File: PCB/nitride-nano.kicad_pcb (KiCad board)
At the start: 6 copper layers, 120 x 57 mm, 323 parts, among them J3 XT-90-M, J4 SWD, J5 SSD1306, J6 XT90-F, P1 USB_C_Plug_USB2.0, Q1 EPC2367, Q10 SQJB90EP-T1_GE3, Q11 AO3404A, Q12 HUASHUO HSBB0115, Q13 AO3404A, Q2 EPC2367, Q3 EPC2367, Q4 EPC2367, Q5 HUASHUO HSBB0115, Q6 AGM612AP, Q8 AO3404A, Q9 AO3404A, SW1 EC11E15244G1, U1 LT8390AIUFD-PBF, U10 SN74LVC1G17DBVR, U11 LMR16006XDDCR, U12 FT234XD, U13 LMR16006XDDCR, U2 STM32G474CEUx, U3 TPD4S480RUKR, U4 TPS26750SRSMR, U5 LM2765, U6 CAT24C512YI-GT3, U7 74LVC1G08SE-7, U8 LTC7004x, U9 INA228AIDGSR, Y1 8M

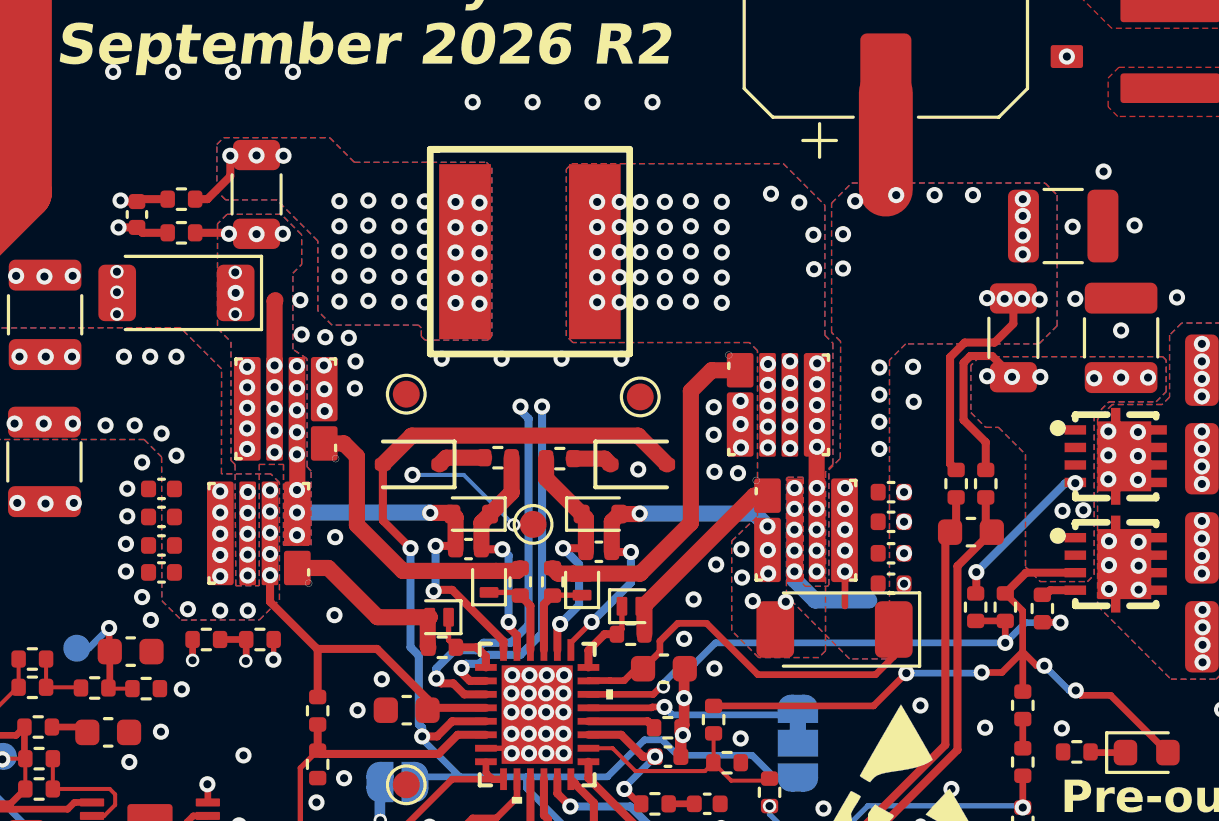
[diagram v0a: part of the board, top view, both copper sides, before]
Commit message: OLED Corruption fix, added UART Boot, DC-losses sim
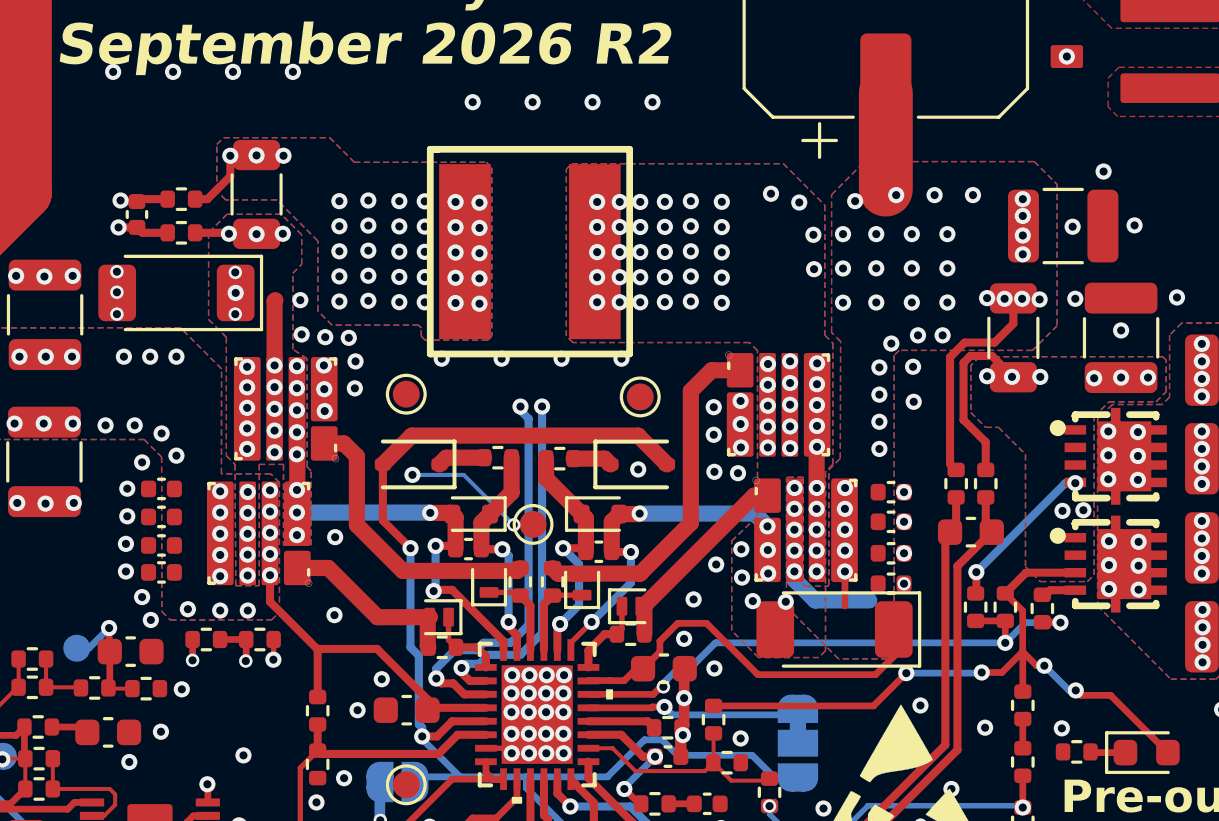
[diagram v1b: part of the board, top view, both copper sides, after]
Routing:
- net Net-(D3-K): vias 28 -> 41
